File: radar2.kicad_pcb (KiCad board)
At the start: 4 copper layers, 126 parts, among them IC1 BQ25713RSNR, IC2 TPS54540DDA, IC3 LP5907QMFX-3.0Q1, IC4 DW3120TR13, IC5 LP5907QMFX-3.0Q1, J1 GSB1C4621DS1HR, J2 M20-8770546 (for SWD), J3 M20-8770342 (for RasPi), J4 JST-XH, J6 SMA_CONNECTOR, J7 SMA_CONNECTOR, Q1 CSD17308Q3, Q2 CSD17308Q3, Q3 CSD17308Q3, Q4 CSD17308Q3, Q5 CSD25404Q3, SW1 09.03290.01, SW2 SWT0220-016016GSA, U1 STM32H725ZETx, Y1 ECS-384-CDX-2482

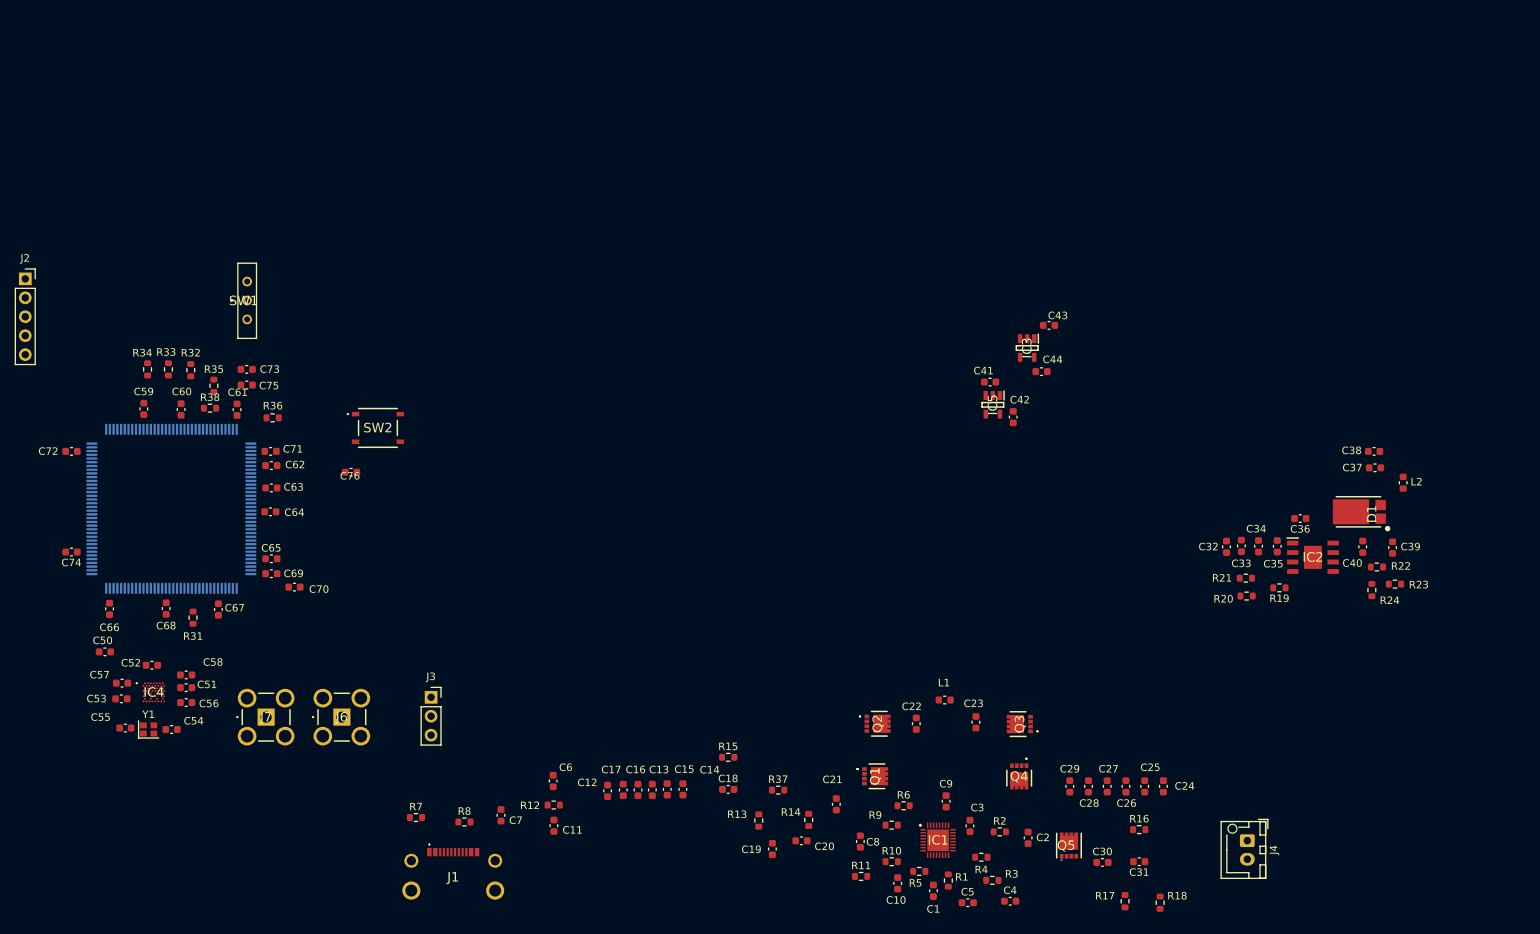
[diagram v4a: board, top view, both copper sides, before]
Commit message: updating schematic from pcb with the power connectors
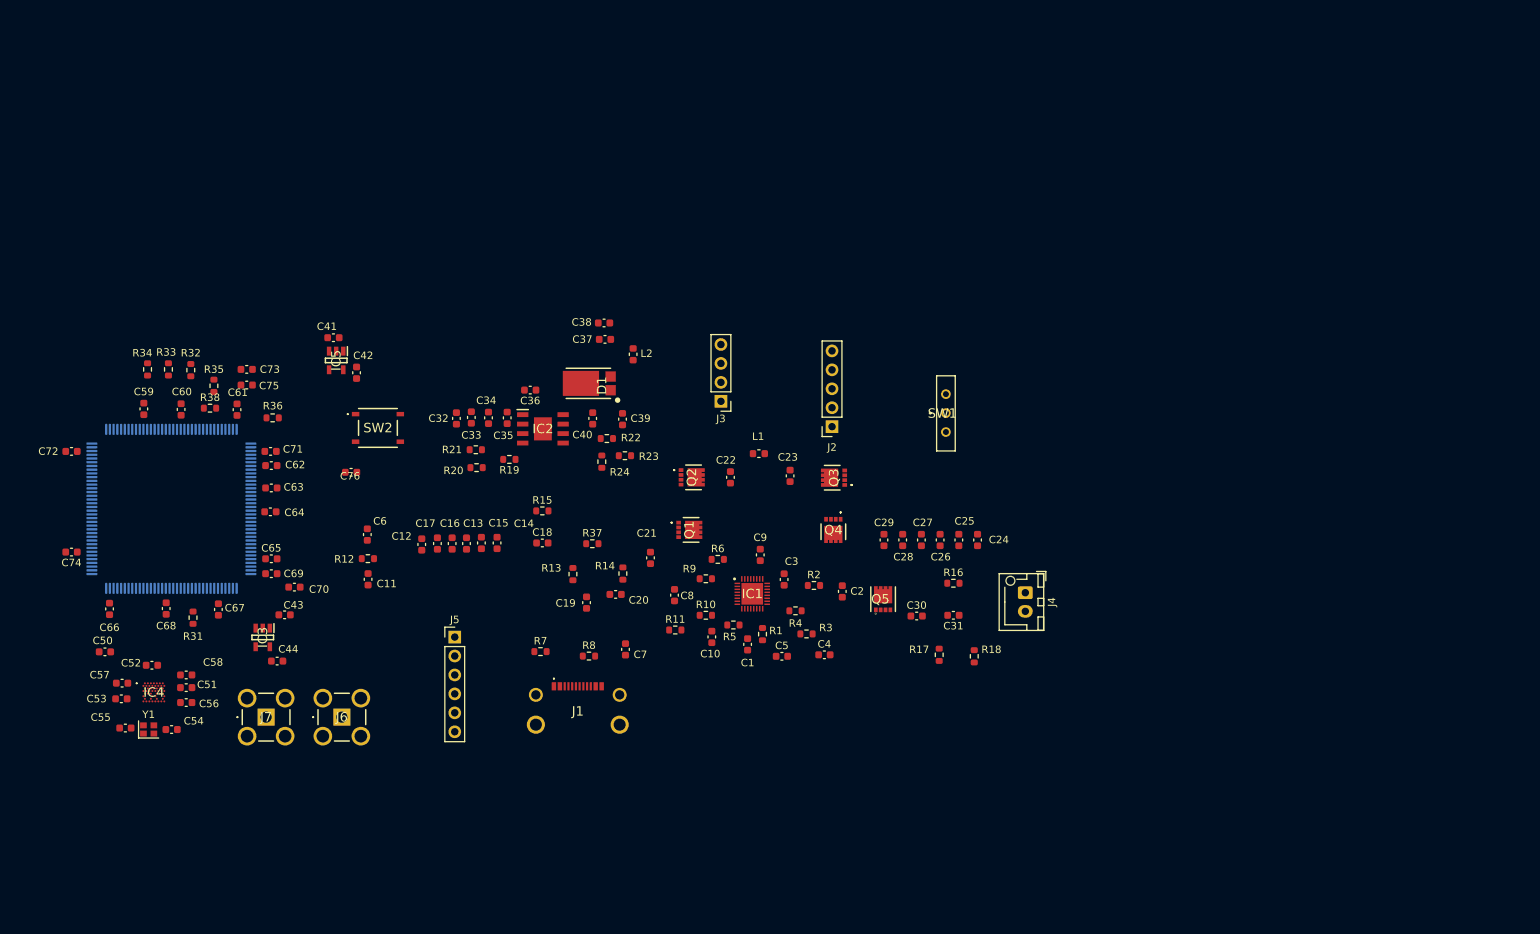
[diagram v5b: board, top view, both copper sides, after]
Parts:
- added J5: M20-9990646_PI, Connector_PinHeader_2.54mm:PinHeader_1x06_P2.54mm_Vertical, F.Cu at (114.2, 118.8)
- J3: value M20-8770342 (for RasPi) -> M20-9730446_DISPLAY_POWER; footprint Connector_PinSocket_2.54mm:PinSocket_1x03_P2.54mm_Vertical -> Connector_PinHeader_2.54mm:PinHeader_1x04_P2.54mm_Vertical
- moved J2 110.0 mm to (164.8, 90.6), turned to 180 degrees
- moved C43 109.6 mm to (91.4, 115.8)
- moved C44 109.6 mm to (90.4, 122.0)
- moved IC3 109.6 mm to (88.5, 118.8)
- moved C34 104.7 mm to (118.7, 89.4)
- moved C37 104.7 mm to (134.3, 78.9)
- moved C38 104.7 mm to (134.2, 76.7)
- moved C39 104.7 mm to (136.7, 89.6)
- moved C40 104.7 mm to (132.7, 89.5)
- moved D1 104.7 mm to (131.1, 84.8)
- moved IC2 104.7 mm to (126.0, 90.9)
- moved L2 104.7 mm to (138.1, 80.9)
- moved R19 104.7 mm to (121.5, 95.0)
- moved R20 104.7 mm to (117.1, 96.1)
- moved R21 104.7 mm to (117.0, 93.7)
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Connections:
- C37 pad 2: VOUT -> VOUT_5V
- C38 pad 2: VOUT -> VOUT_5V
- C41 pad 2: VOUT -> VOUT_5V
- C43 pad 2: VOUT -> VOUT_5V
- IC3 pad 1: VOUT -> VOUT_5V
- IC3 pad 3: VOUT -> VOUT_5V
- IC5 pad 1: VOUT -> VOUT_5V
- IC5 pad 3: VOUT -> VOUT_5V
- J3 pad 1: SW_USART2_TX -> VOUT_5V
- J3 pad 2: SW_USART2_RX -> GND
- J3 pad 3: GND -> VOUT_5V
- L2 pad 2: VOUT -> VOUT_5V
- R23 pad 1: VOUT -> VOUT_5V

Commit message: almost ready for routing
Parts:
- U1: moved to F.Cu
- moved IC3 60.5 mm to (121.5, 68.1)
- moved C44 30.6 mm to (116.3, 105.7), turned to -90 degrees
- moved C7 30.2 mm to (162.7, 104.5)
- moved R8 29.3 mm to (157.0, 105.8)
- moved C43 28.3 mm to (116.6, 102.9)
- moved J1 28.2 mm to (154.6, 113.9)
- moved C14 27.8 mm to (143.8, 91.9)
- moved C1 27.8 mm to (177.3, 105.4)
- moved C19 27.8 mm to (155.7, 99.8)
- moved C20 27.8 mm to (159.6, 98.7)
- moved C21 27.8 mm to (164.2, 93.8)
- moved C24 27.8 mm to (208.1, 91.4)
- moved C25 27.8 mm to (205.6, 91.4)
- moved C26 27.8 mm to (203.1, 91.4)
- moved C27 27.8 mm to (200.6, 91.4)
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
